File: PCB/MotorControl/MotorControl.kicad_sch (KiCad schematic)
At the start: 14 parts, among them J1 USB_C_Receptacle_USB2.0_14P, J2 Conn_02x05_Top_Bottom, J3 Conn_01x06, J4 Conn_01x03, SW1 SW_Push, U1 STM32L031K6Tx, U2 TC1262-33

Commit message: wasd
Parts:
- removed C1: .1uf, Capacitor_SMD:C_0805_2012Metric_Pad1.18x1.45mm_HandSolder, symbol Device:C
- removed C2: 10uf, Capacitor_SMD:C_0805_2012Metric_Pad1.18x1.45mm_HandSolder, symbol Device:C
- removed D1, D2: LED, LED_SMD:LED_0805_2012Metric_Pad1.15x1.40mm_HandSolder, symbol Device:LED
- removed J1: USB_C_Receptacle_USB2.0_14P, Connector_USB:USB_C_Receptacle_GCT_USB4085, symbol Connector:USB_C_Receptacle_USB2.0_14P
- removed J2: Conn_02x05_Top_Bottom, Connector_PinHeader_2.54mm:PinHeader_2x05_P2.54mm_Vertical, symbol Connector_Generic:Conn_02x05_Top_Bottom
- removed J3: Conn_01x06, Connector_PinHeader_2.54mm:PinHeader_1x06_P2.54mm_Vertical, symbol Connector_Generic:Conn_01x06
- removed J4: Conn_01x03, Connector_PinHeader_2.54mm:PinHeader_1x03_P2.54mm_Vertical, symbol Connector_Generic:Conn_01x03
- removed R1: 4.7k, Resistor_SMD:R_0805_2012Metric_Pad1.20x1.40mm_HandSolder, symbol Device:R
- removed R2, R3: 330, Resistor_SMD:R_0805_2012Metric_Pad1.20x1.40mm_HandSolder, symbol Device:R
- removed SW1: SW_Push, Button_Switch_THT:SW_PUSH_6mm_H4.3mm, symbol Switch:SW_Push
- removed U1: STM32L031K6Tx, Package_QFP:LQFP-32_7x7mm_P0.8mm, symbol MCU_ST_STM32L0:STM32L031K6Tx
- removed U2: TC1262-33, Package_TO_SOT_SMD:SOT-223-3_TabPin2, symbol Regulator_Linear:TC1262-33
- added C3: 1, Capacitor_SMD:C_0504_1310Metric_Pad0.83x1.28mm_HandSolder, symbol Device:C
- added C4: .1u, Capacitor_SMD:C_0504_1310Metric_Pad0.83x1.28mm_HandSolder, symbol Device:C
- added D3: LED, LED_SMD:LED_1206_3216Metric_Pad1.42x1.75mm_HandSolder, symbol Device:LED
- added J5: Conn_01x05_Pin, Connector_PinHeader_1.00mm:PinHeader_1x05_P1.00mm_Vertical, symbol Connector:Conn_01x05_Pin
- added J6: USB_C_Receptacle_USB2.0_14P, Connector_USB:USB_C_Receptacle_GCT_USB4085, symbol Connector:USB_C_Receptacle_USB2.0_14P
- added J8: Conn_01x04_Socket, Connector_PinHeader_1.00mm:PinHeader_1x04_P1.00mm_Horizontal, symbol Connector:Conn_01x04_Socket
- added R4: 270, Resistor_SMD:R_0805_2012Metric_Pad1.20x1.40mm_HandSolder, symbol Device:R
- added U1: PCA9685PW, Package_SO:TSSOP-28_4.4x9.7mm_P0.65mm, symbol Driver_LED:PCA9685PW
- added U3: TC1262-33, Package_TO_SOT_SMD:SOT-223-3_TabPin2, symbol Regulator_Linear:TC1262-33
- added U4: STM32L031K6Tx, Package_QFP:LQFP-32_7x7mm_P0.8mm, symbol MCU_ST_STM32L0:STM32L031K6Tx
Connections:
- net +3.3V: now also C3.1, C4.1, J5.1 (Pin_1), R4.1, U3.3 (VO), U4.1 (VDD), U4.17 (VDD), U4.5 (VDDA)
- net +5V: now also J6.A4 (VBUS), J6.A9 (VBUS), J6.B4 (VBUS), J6.B9 (VBUS), J8.4 (Pin_4), U3.1 (VI)
- net GND: now also C3.2, C4.2, D3.1 (K), J5.2 (Pin_2), J6.A1 (GND), J6.A12 (GND), J6.B1 (GND), J6.B12 (GND), J8.3 (Pin_3), U3.2 (GND), U4.16 (VSS), U4.31 (BOOT0), U4.32 (VSS)
- net NRST: now also J5.5 (Pin_5), U4.4 (NRST)
- new net: D3.2 (A), R4.2
- new net RX: J8.1 (Pin_1), U4.9 (PA3)
- new net SWDIO: J5.4 (Pin_4), U4.23 (PA13)
- new net SWSCLK: J5.3 (Pin_3), U4.24 (PA14)
- new net TX: J8.2 (Pin_2), U4.8 (PA2)
- no-connect marks 33 -> 23

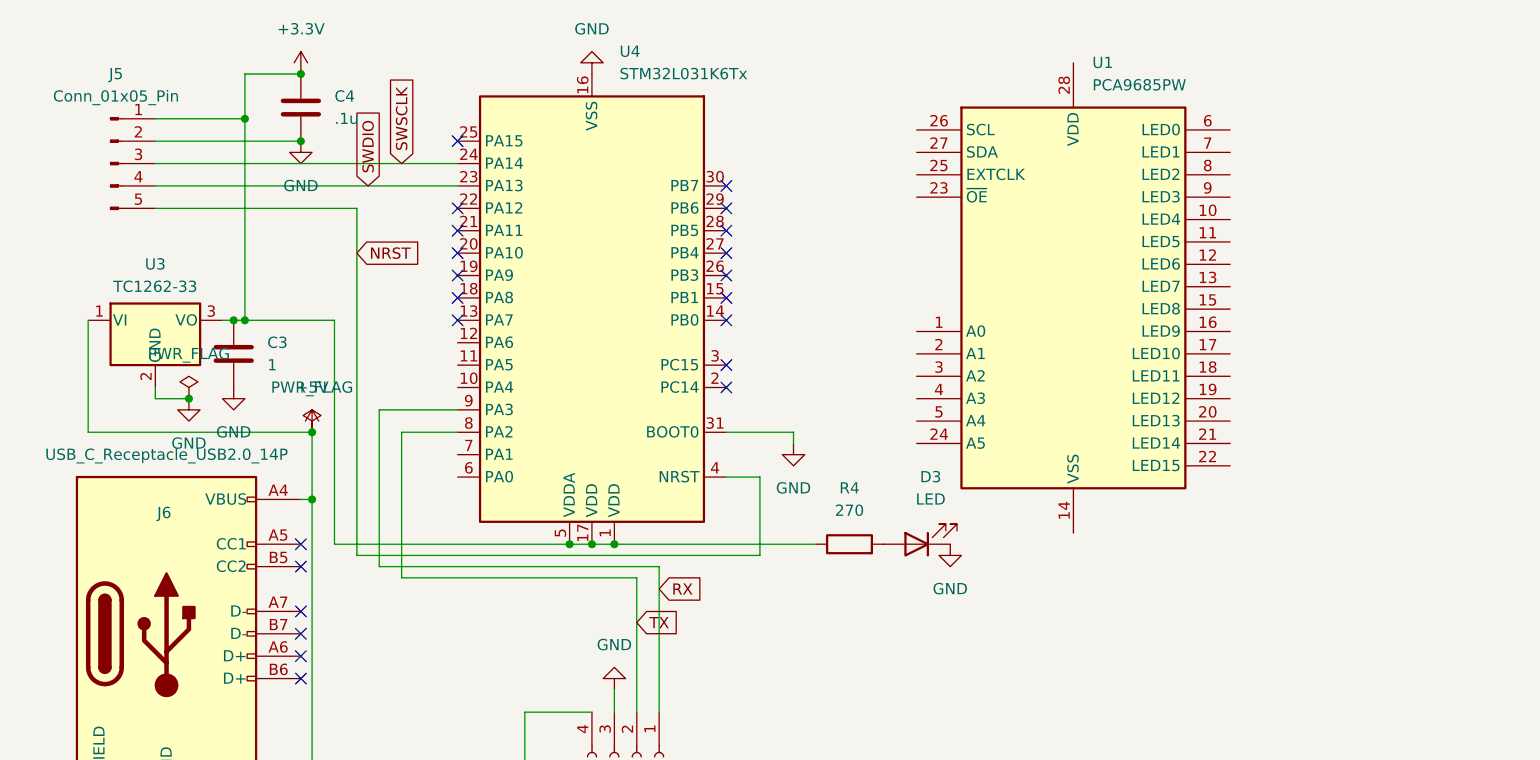
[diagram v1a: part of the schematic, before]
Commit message: Routing for motor control PCB
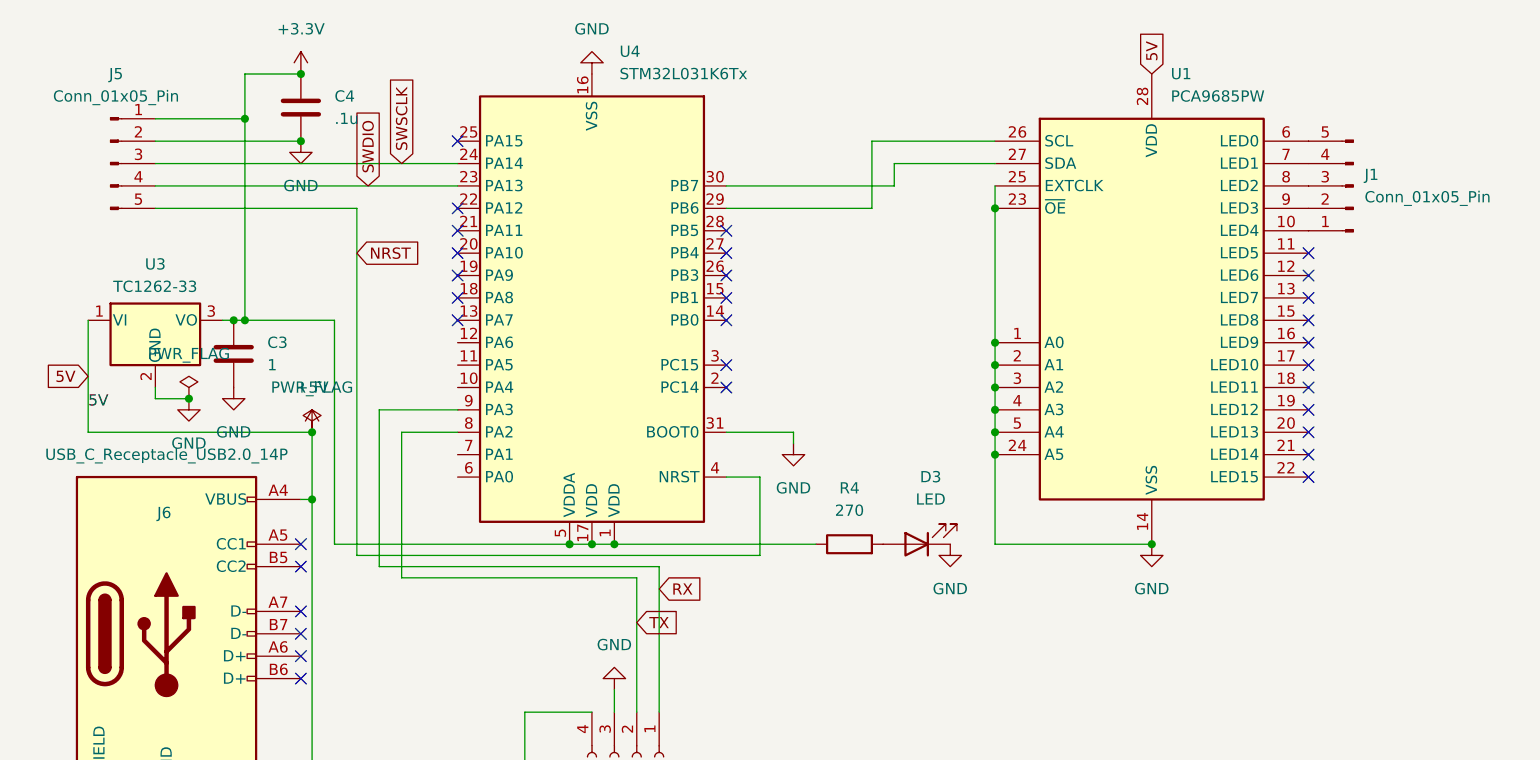
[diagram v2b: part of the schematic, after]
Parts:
- added J1: Conn_01x05_Pin, Connector_PinHeader_1.00mm:PinHeader_1x05_P1.00mm_Vertical, symbol Connector:Conn_01x05_Pin
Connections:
- net +5V: now also U1.28 (VDD)
- net GND: now also U1.1 (A0), U1.14 (VSS), U1.2 (A1), U1.23 (~{OE}), U1.24 (A5), U1.25 (EXTCLK), U1.3 (A2), U1.4 (A3), U1.5 (A4)
- net at U1.10 (LED4): now also J1.1 (Pin_1)
- net at U1.26 (SCL): now also U4.29 (PB6)
- net at U1.27 (SDA): now also U4.30 (PB7)
- net at U1.6 (LED0): now also J1.5 (Pin_5)
- net at U1.7 (LED1): now also J1.4 (Pin_4)
- net at U1.8 (LED2): now also J1.3 (Pin_3)
- net at U1.9 (LED3): now also J1.2 (Pin_2)
- no-connect marks 23 -> 32
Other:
- moved on the sheet: U1

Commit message: Pushing
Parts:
- removed J1: Conn_01x05_Pin, Connector_PinHeader_1.00mm:PinHeader_1x05_P1.00mm_Vertical, symbol Connector:Conn_01x05_Pin
- removed J8: Conn_01x04_Socket, Connector_PinHeader_1.00mm:PinHeader_1x04_P1.00mm_Horizontal, symbol Connector:Conn_01x04_Socket
- added J1, J2, J3, J4, J7: Conn_01x03_Pin, Connector_PinHeader_2.54mm:PinHeader_1x03_P2.54mm_Horizontal, symbol Connector:Conn_01x03_Pin
- added U2: NORA-W106-00B, NORA-W106-00B:XCVR_NORA-W106-00B, symbol NORA-W106-00B:NORA-W106-00B
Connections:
- net +3.3V: now also U2.A8 (VCC)
- net +5V: now also J1.2 (Pin_2), J2.2 (Pin_2), J3.2 (Pin_2), J4.2 (Pin_2), J7.2 (Pin_2)
- net GND: now also J1.1 (Pin_1), J2.1 (Pin_1), J3.1 (Pin_1), J4.1 (Pin_1), J7.1 (Pin_1), U2.A1 (EGP), U2.A9 (EGP), U2.B2 (EGP), U2.B8 (EGP), U2.E4 (EGP), U2.E5 (EGP), U2.F4 (EGP), U2.F5 (EGP), U2.K2 (EGP), U2.K3 (EGP), U2.K5 (EGP), U2.K7 (EGP), U2.K8 (EGP)
- net RX: now also U2.G9 (U0RXD/GPIO44)
- net TX: now also U2.G8 (U0TXD/GPIO43)
- net at U1.10 (LED4): now also J1.3 (Pin_3)
- net at U1.9 (LED3): now also J2.3 (Pin_3)
- net at U1.8 (LED2): now also J3.3 (Pin_3)
- net at U1.7 (LED1): now also J4.3 (Pin_3)
- net at U1.6 (LED0): now also J7.3 (Pin_3)
- new net: U2.A4 (NC), U2.B5 (NC), U2.B9 (NC), U2.C5 (NC), U2.D7 (NC), U2.G4 (NC), U2.G5 (NC), U2.G7 (NC), U2.J4 (NC), U2.J5 (NC), U2.J7 (NC), U2.K1 (NC)
- new net: U2.A7 (VCCIO), U2.B7 (VCCIO)
- new net: U2.L1 (EAGP), U2.L9 (EAGP), U2.M1 (EAGP), U2.M2 (EAGP), U2.M8 (EAGP), U2.M9 (EAGP)
- no-connect marks 32 -> 81

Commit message: Pushing updated servo controller
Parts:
- added D1, D2: LED, LED_SMD:LED_1206_3216Metric_Pad1.42x1.75mm_HandSolder, symbol Device:LED
- added H1, H2, H3: MountingHole_Pad, MountingHole:MountingHole_4.5mm_Pad, symbol Mechanical:MountingHole_Pad
- added J8: Conn_01x02_Pin, Connector_PinHeader_2.54mm:PinHeader_1x02_P2.54mm_Vertical, symbol Connector:Conn_01x02_Pin
- added R1, R2: R, Resistor_SMD:R_0805_2012Metric_Pad1.20x1.40mm_HandSolder, symbol Device:R
- J5: footprint Connector_PinHeader_1.00mm:PinHeader_1x05_P1.00mm_Vertical -> Connector_PinHeader_2.54mm:PinHeader_1x05_P2.54mm_Vertical
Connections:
- net NRST is gone; now on net Debug_rx: J5.5 (Pin_5), U4.4 (NRST)
- net +3.3V: now also U1.28 (VDD)
- net +5V: no longer U1.28 (VDD)
- net GND: now also D1.1 (K), D2.1 (K)
- net Motor1PWM: now reaches J1.3 (Pin_3), U1.10 (LED4)
- net Motor1PWM: now also H1.1
- net MotorControl_SCL: now reaches U1.26 (SCL), U4.29 (PB6)
- net MotorControl_SCL: now also H3.1
- net DebugTX: now reaches U2.A5 (FSPIDQS/GPIO14)
- net DebugTX: now also H2.1
- net Switch2: now reaches U2.C8 (GPIO21)
- net Switch2: now also U4.27 (PB4)
- net Switch1: now reaches U2.D8 (GPIO4)
- net Switch1: now also U4.28 (PB5)
- net BlueLED: now reaches U2.H9 (GPIO8)
- net BlueLED: now also R1.1
- net at U2.J3 (~{RESET}): now also U4.13 (PA7)
- net RedLED: now reaches U2.J8 (GPIO5)
- net RedLED: now also R2.2
- net GPIO_J9: now reaches U2.J9 (GPIO3)
- net GPIO_J9: now also U4.26 (PB3)
- net Debug_tx: now reaches U4.19 (PA9)
- net Debug_tx: now also J8.2 (Pin_2)
- net Debug_rx: now reaches U4.20 (PA10)
- net Debug_rx: now also J8.1 (Pin_1)
- new net: D2.2 (A), R2.1
- new net: D1.2 (A), R1.2
- no-connect marks 81 -> 73

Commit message: Motor
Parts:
- removed D1, D2: LED, LED_SMD:LED_1206_3216Metric_Pad1.42x1.75mm_HandSolder, symbol Device:LED
- removed H1, H2, H3: MountingHole_Pad, MountingHole:MountingHole_4.5mm_Pad, symbol Mechanical:MountingHole_Pad
- removed J8: Conn_01x02_Pin, Connector_PinHeader_2.54mm:PinHeader_1x02_P2.54mm_Vertical, symbol Connector:Conn_01x02_Pin
- removed R1: R, Resistor_SMD:R_0805_2012Metric_Pad1.20x1.40mm_HandSolder, symbol Device:R
- added D1: ASMB-MTB0-0A3A2, LED_SMD:LED_Avago_PLCC4_3.2x2.8mm_CW, symbol LED:ASMB-MTB0-0A3A2
- added J9: Conn_01x06_Socket, Connector_PinSocket_2.54mm:PinSocket_1x06_P2.54mm_Vertical, symbol Connector:Conn_01x06_Socket
- added TP1, TP2, TP3: TestPoint, TestPoint:TestPoint_Pad_2.5x2.5mm, symbol Connector:TestPoint
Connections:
- net BlueLED: now also D1.2 (BK)
- net DebugTX: now also TP3.1
- net Debug_rx: now also U4.19 (PA9), J9.5 (Pin_5); no longer J5.5 (Pin_5), U4.20 (PA10), U4.4 (NRST)
- net Debug_tx: now also J5.5 (Pin_5), U4.20 (PA10), U4.4 (NRST), J9.4 (Pin_4); no longer U4.19 (PA9)
- net GND: now also R2.1, J9.1 (Pin_1)
- net Motor1PWM: now also TP2.1
- net MotorControl_SCL: now also TP1.1
- net RedLED: now also D1.4 (RK); no longer R2.2
- new net: D1.1 (A), R2.2
- no-connect marks 73 -> 77
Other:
- moved on the sheet: R2

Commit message: wasd
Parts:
- added C1, C2, C5, C6, C7: C, Capacitor_SMD:C_0504_1310Metric_Pad0.83x1.28mm_HandSolder, symbol Device:C
- added D2: LED, LED_SMD:LED_1206_3216Metric_Pad1.42x1.75mm_HandSolder, symbol Device:LED
- added R1: 270, Resistor_SMD:R_0805_2012Metric_Pad1.20x1.40mm_HandSolder, symbol Device:R
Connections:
- net +3.3V: now also U2.A7 (VCCIO), U2.B7 (VCCIO), C1.1, C2.1, C5.1, C6.1, C7.2
- net GND: now also C1.2, C2.2, C5.2, C6.2, C7.1, D2.1 (K)
- net RX: now also U2.G8 (U0TXD/GPIO43); no longer U2.G9 (U0RXD/GPIO44)
- net TX: now also U2.G9 (U0RXD/GPIO44); no longer U2.G8 (U0TXD/GPIO43)
- net GreenLED: now reaches D1.3 (GK)
- net GreenLED: now also U2.H8 (GPIO2)
- net UART_RTS->Board_CTS: now reaches U2.F8 (GPIO45)
- net UART_RTS->Board_CTS: now also U4.21 (PA11)
- net UART_CTS->Board_RTS: now reaches U2.F9 (GPIO6)
- net UART_CTS->Board_RTS: now also U4.14 (PB0)
- net HeartBeat: now reaches U4.15 (PB1)
- net HeartBeat: now also R1.2
- new net: D2.2 (A), R1.1
- no-connect marks 77 -> 69

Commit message: wasd
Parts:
- added J10: Conn_01x01_Pin, Connector_PinHeader_2.54mm:PinHeader_1x01_P2.54mm_Vertical, symbol Connector:Conn_01x01_Pin
- added J8: Barrel_Jack, Connector_BarrelJack:BarrelJack_CUI_PJ-063AH_Horizontal, symbol Connector:Barrel_Jack
- added R3: 270, Resistor_SMD:R_0805_2012Metric_Pad1.20x1.40mm_HandSolder, symbol Device:R
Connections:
- net +5V: now also J8.1
- net GND: now also J8.2, R3.1; no longer U4.31 (BOOT0)
- new net Boot: J10.1 (Pin_1), R3.2, U4.31 (BOOT0)

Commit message: final boards
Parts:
- removed J6: USB_C_Receptacle_USB2.0_14P, Connector_USB:USB_C_Receptacle_GCT_USB4085, symbol Connector:USB_C_Receptacle_USB2.0_14P
- added J6: Conn_01x02_Socket, Connector_PinSocket_2.54mm:PinSocket_1x02_P2.54mm_Horizontal, symbol Connector:Conn_01x02_Socket
- J8: footprint Connector_BarrelJack:BarrelJack_CUI_PJ-063AH_Horizontal -> Connector_BarrelJack:BarrelJack_Wuerth_694106106102_2.0x5.5mm
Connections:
- net +3.3V: now also R2.1
- net +5V: now also J6.1 (Pin_1)
- net GND: now also U2.L1 (EAGP), U2.L9 (EAGP), U2.M1 (EAGP), U2.M2 (EAGP), U2.M8 (EAGP), U2.M9 (EAGP), J6.2 (Pin_2); no longer R2.1
- no-connect marks 69 -> 61
